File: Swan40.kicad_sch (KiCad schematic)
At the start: 92 parts, among them SW1 SW_PUSH, SW10 SW_PUSH, SW11 SW_PUSH, SW12 SW_PUSH, SW13 SW_PUSH, SW14 SW_PUSH, SW15 SW_PUSH, SW16 SW_PUSH, SW17 SW_DPDT_x2, SW18 SW_PUSH, SW19 SW_PUSH, SW2 SW_PUSH, SW20 SW_PUSH, SW21 SW_PUSH, SW22 SW_PUSH, SW23 SW_PUSH, SW24 SW_PUSH, SW25 SW_PUSH, SW26 SW_PUSH, SW27 SW_PUSH, SW28 SW_PUSH, SW29 SW_PUSH, SW3 SW_PUSH, SW30 SW_PUSH, SW31 SW_PUSH, SW32 SW_PUSH, SW33 SW_PUSH, SW34 SW_DPDT_x2, SW35 SW_PUSH, SW36 SW_PUSH, SW37 SW_PUSH, SW38 SW_PUSH, SW39 SW_PUSH, SW4 SW_PUSH, SW40 SW_PUSH, SW41 SW_PUSH, SW42 SW_PUSH, SW5 SW_PUSH, SW6 SW_PUSH, SW7 SW_PUSH, SW8 SW_PUSH, SW9 SW_PUSH, U1 xiao_nrf52840, U2 xiao_nrf52840

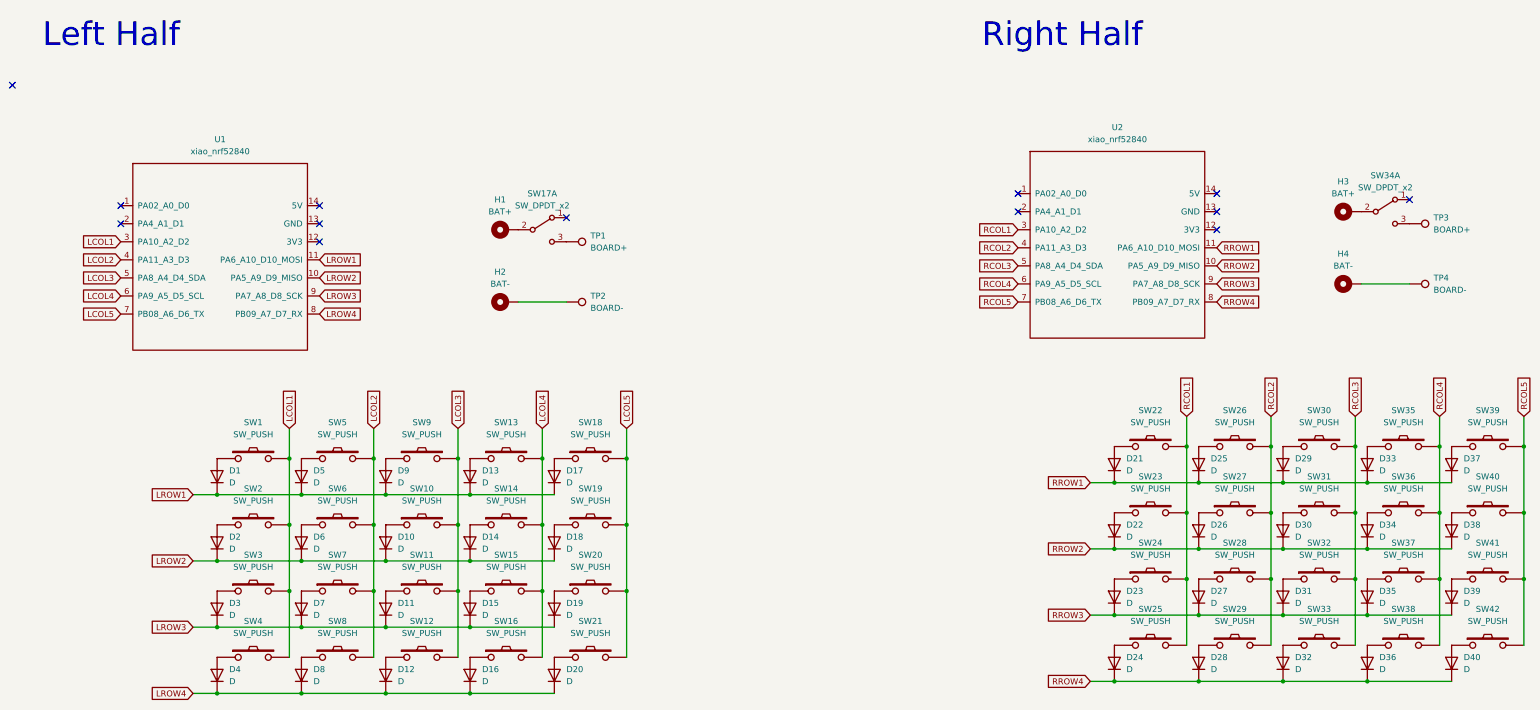
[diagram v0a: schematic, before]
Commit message: Designed + Export automation (#1)
* Base wiring completed

* Updated board outline

* Wiring complete

* Fixed errors + Rounded tracks

* Rounded + added droplets + fill zones

* Added base kibot automation

* Fixed workflow

* Attempted fix

* Switched to rounded file

* Attempted fix

* Fixed typo

* Updated readme

* Runs action every time

* Everything re-aligned and re-wired

* Updated violations

* Added mouse bites

* Fixed schematic warnings

* Fixed JLCPCB config

* Removed everything from JLCPCB config besides gerber and drill files
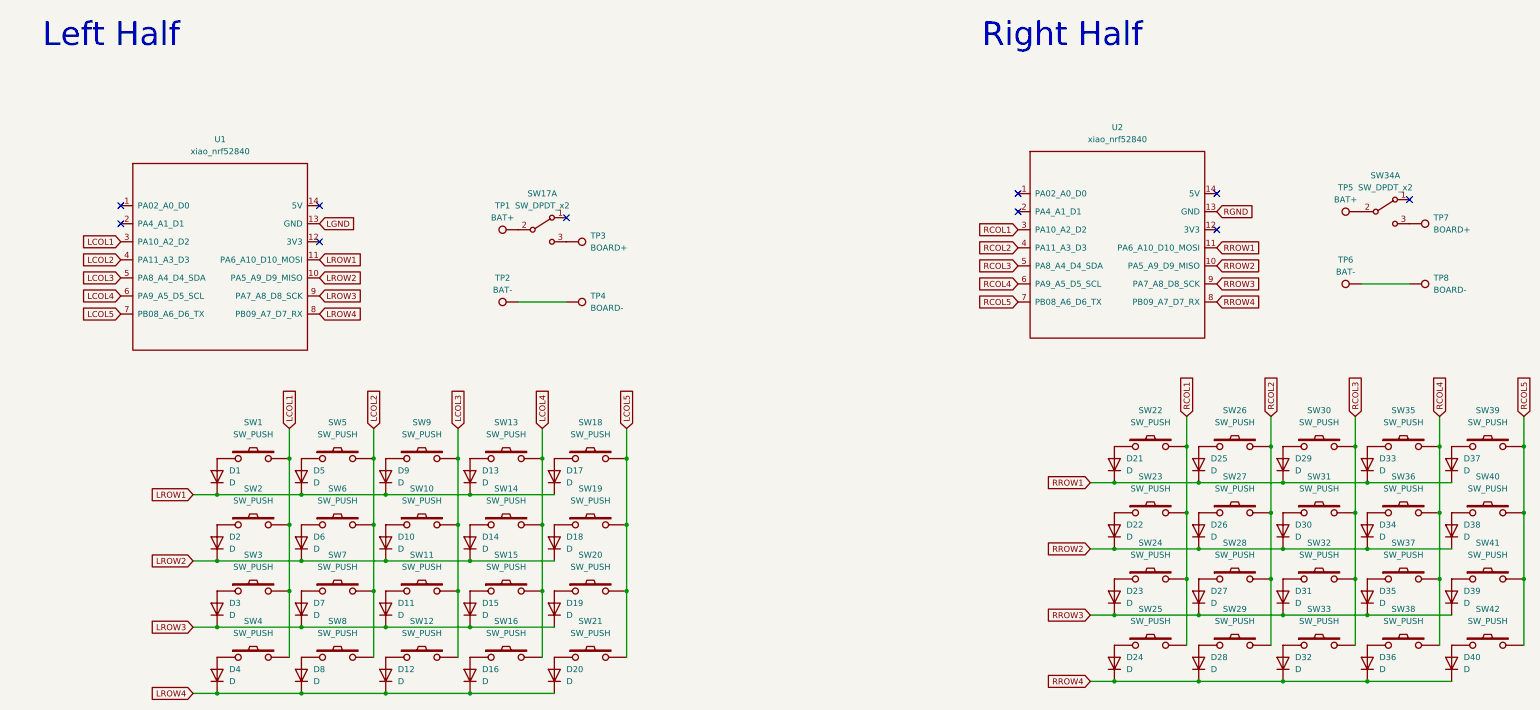
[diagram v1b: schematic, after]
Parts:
- removed H1, H3: BAT+, kbd:1pin_conn, symbol Mechanical:MountingHole_Pad
- removed H2, H4: BAT-, kbd:1pin_conn, symbol Mechanical:MountingHole_Pad
- added TP1, TP5: BAT+, kbd:1pad_conn_board, symbol Connector:TestPoint
- added TP2, TP6: BAT-, kbd:1pad_conn_board, symbol Connector:TestPoint
- U1, U2: footprint xiao_nrf52840:xiao_nrf52840 -> xiao_nrf52840:xiao_nrf52840_v2
- renumbered TP1 to TP3, TP2 to TP4, TP3 to TP7, TP4 to TP8
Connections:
- net at TP8.1: now also TP6.1
- net LGND: now reaches U1.13 (GND)
- net at SW34.2 (B): now also TP5.1
- net at SW17.2 (B): now also TP1.1
- net RGND: now reaches U2.13 (GND)
- net at TP4.1: now also TP2.1
- no-connect marks 13 -> 10
